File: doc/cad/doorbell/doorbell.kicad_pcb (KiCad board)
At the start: 2 copper layers, 128.5 x 91.5 mm, 32 parts, among them J1 Bell PCB Conn, J2 +12VDC, J3 Speaker, J4 UART, T1 Transformer_1P_1S, U1 ESP32-WROOM-32, U2 TDA1517P/N3_112, U3 AMS1117-3.3

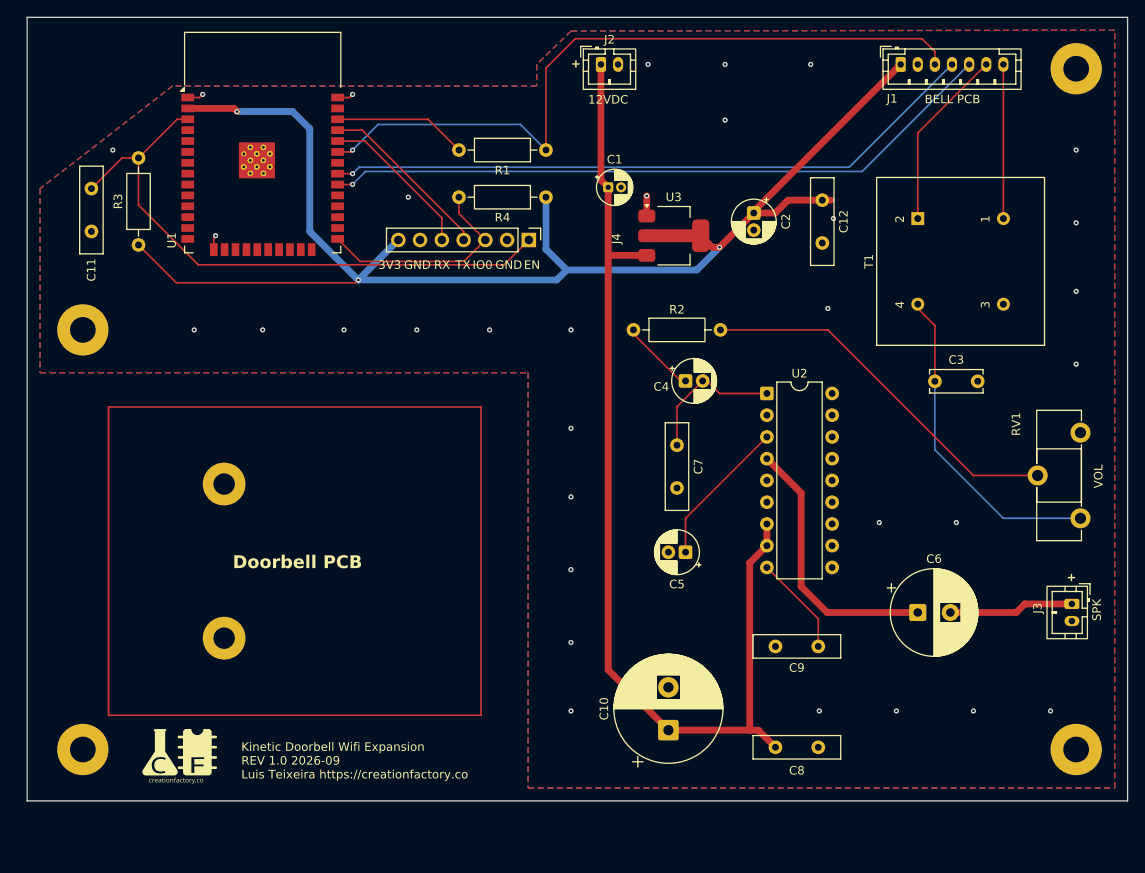
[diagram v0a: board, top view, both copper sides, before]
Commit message: Copper area improvements
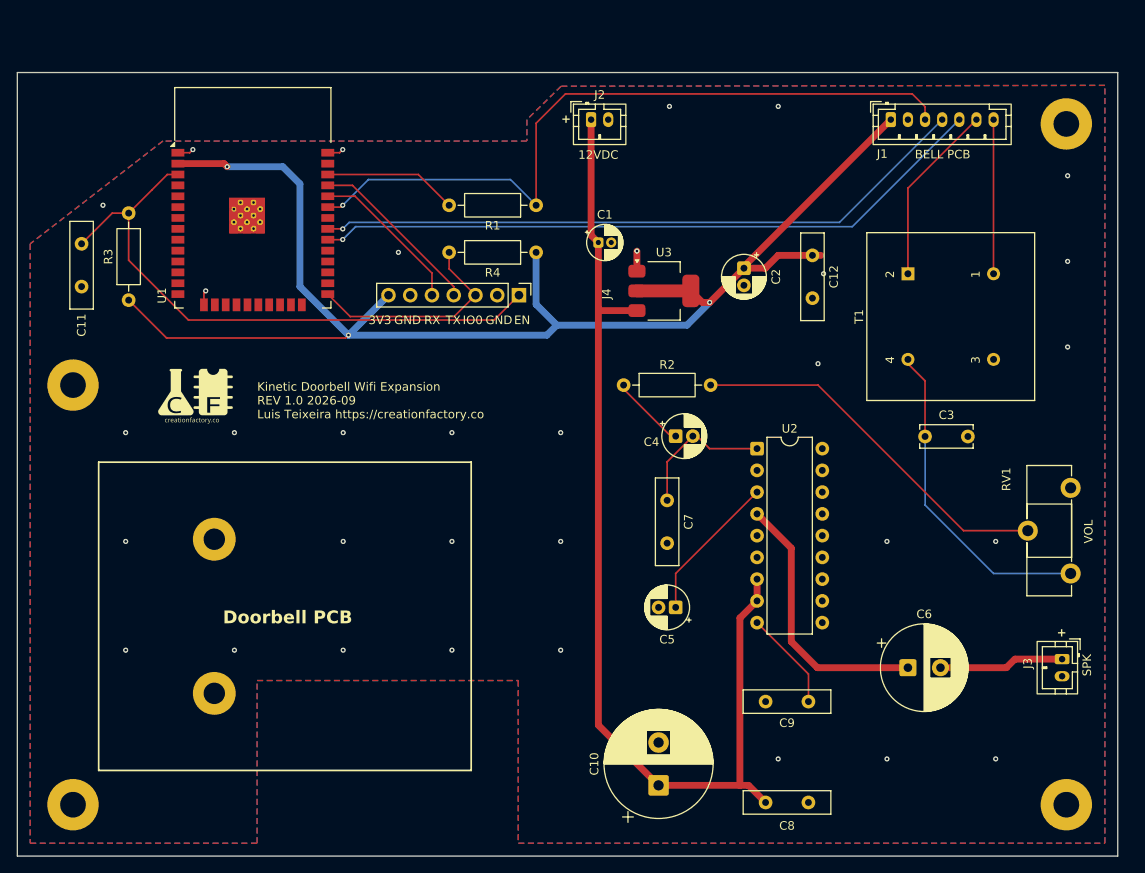
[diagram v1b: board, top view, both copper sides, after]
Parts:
- J1: value Bell PCB Conn -> Doorbell PCB
- J2: value +12VDC -> 12V Supply
- moved G*** 42.1 mm to (108.3, 80.4)
- moved C10 6.55 mm to (162.2, 126.2)
- moved C4 6.55 mm to (164.2, 85.4)
- moved C5 6.55 mm to (164.2, 105.4)
- moved C7 6.55 mm to (163.2, 92.9)
- moved C8 6.55 mm to (179.7, 128.2)
- moved C9 6.55 mm to (179.7, 116.4)
- moved R3 6.55 mm to (100.3, 69.5)
- moved C1 6.55 mm to (155.2, 62.8)
- moved C11 6.55 mm to (94.8, 62.9)
- moved C12 6.55 mm to (180.2, 64.3)
- moved C2 6.55 mm to (172.2, 65.8)
- moved J1 6.55 mm to (189.3, 48.4)
- moved J2 6.55 mm to (154.3, 48.4)
- moved R1 6.55 mm to (147.9, 58.4)
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- renumbered REF** to DB_PCB_01, REF** to DB_PCB_02, REF** to LB_HOLE, REF** to LT_HOLE, REF** to RB_HOLE, REF** to RT_HOLE
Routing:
- net GND: vias 33 -> 32
